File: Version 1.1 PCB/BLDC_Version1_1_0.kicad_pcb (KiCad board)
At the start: 2 copper layers, 80 x 80 mm, 122 parts, among them CN1 DB910-7.62-3P, CN2 XT60PW-M, CN3 SM06B-GHS-TB(LF)(SN), J1 USB_C_Receptacle_USB2.0_14P, Q1 N_FET_ISC0602NLS, Q2 N_FET_ISC0602NLS, Q3 SI7129DN-T1-GE3, Q4 N_FET_ISC0602NLS, Q5 N_FET_ISC0602NLS, Q6 N_FET_ISC0602NLS, Q7 N_FET_ISC0602NLS, SW1 SW_MEC_5E, SW2 SW_MEC_5E, U1 ESP32-S3-WROOM-1, U10 SRV05-4-HXY, U11 SRV05-4-HXY, U13 SRV05-4-HXY, U14 SRV05-4-HXY, U2 AP7363-33D-13, U3 TMC6200-TA-T, U4 TPS5430DDAR, U5 SM03B-GHS-TB(LF)(SN), U7 8x Male Headers, U9 Male Headers

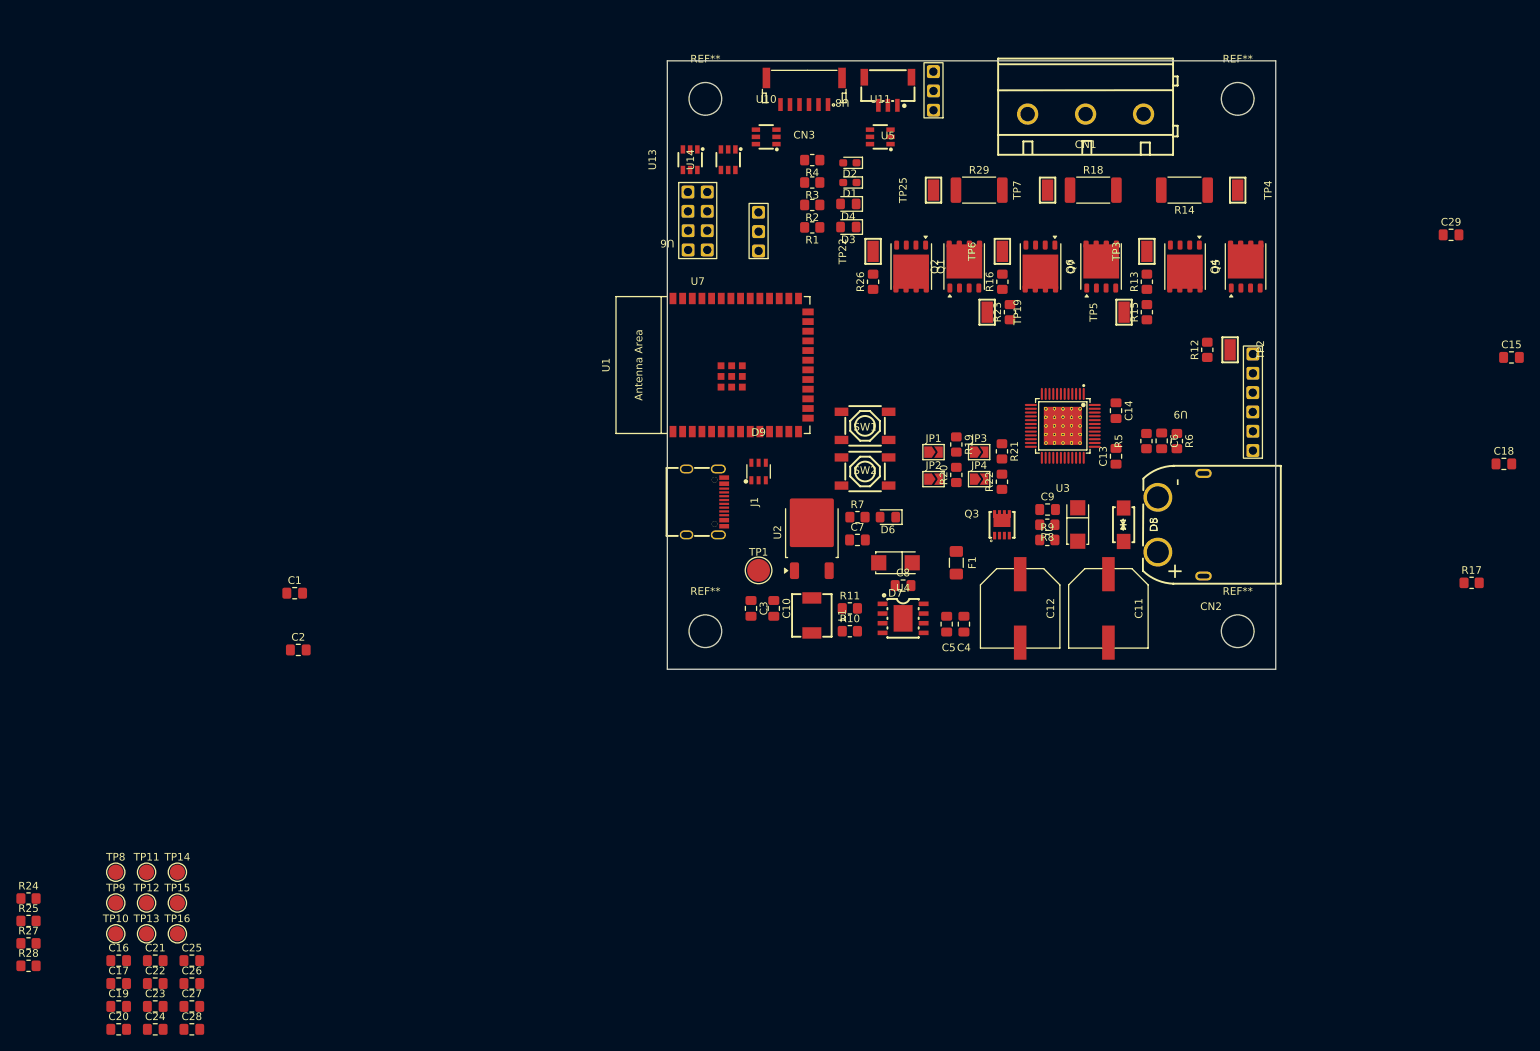
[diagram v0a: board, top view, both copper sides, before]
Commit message: Completed Placement of Parts
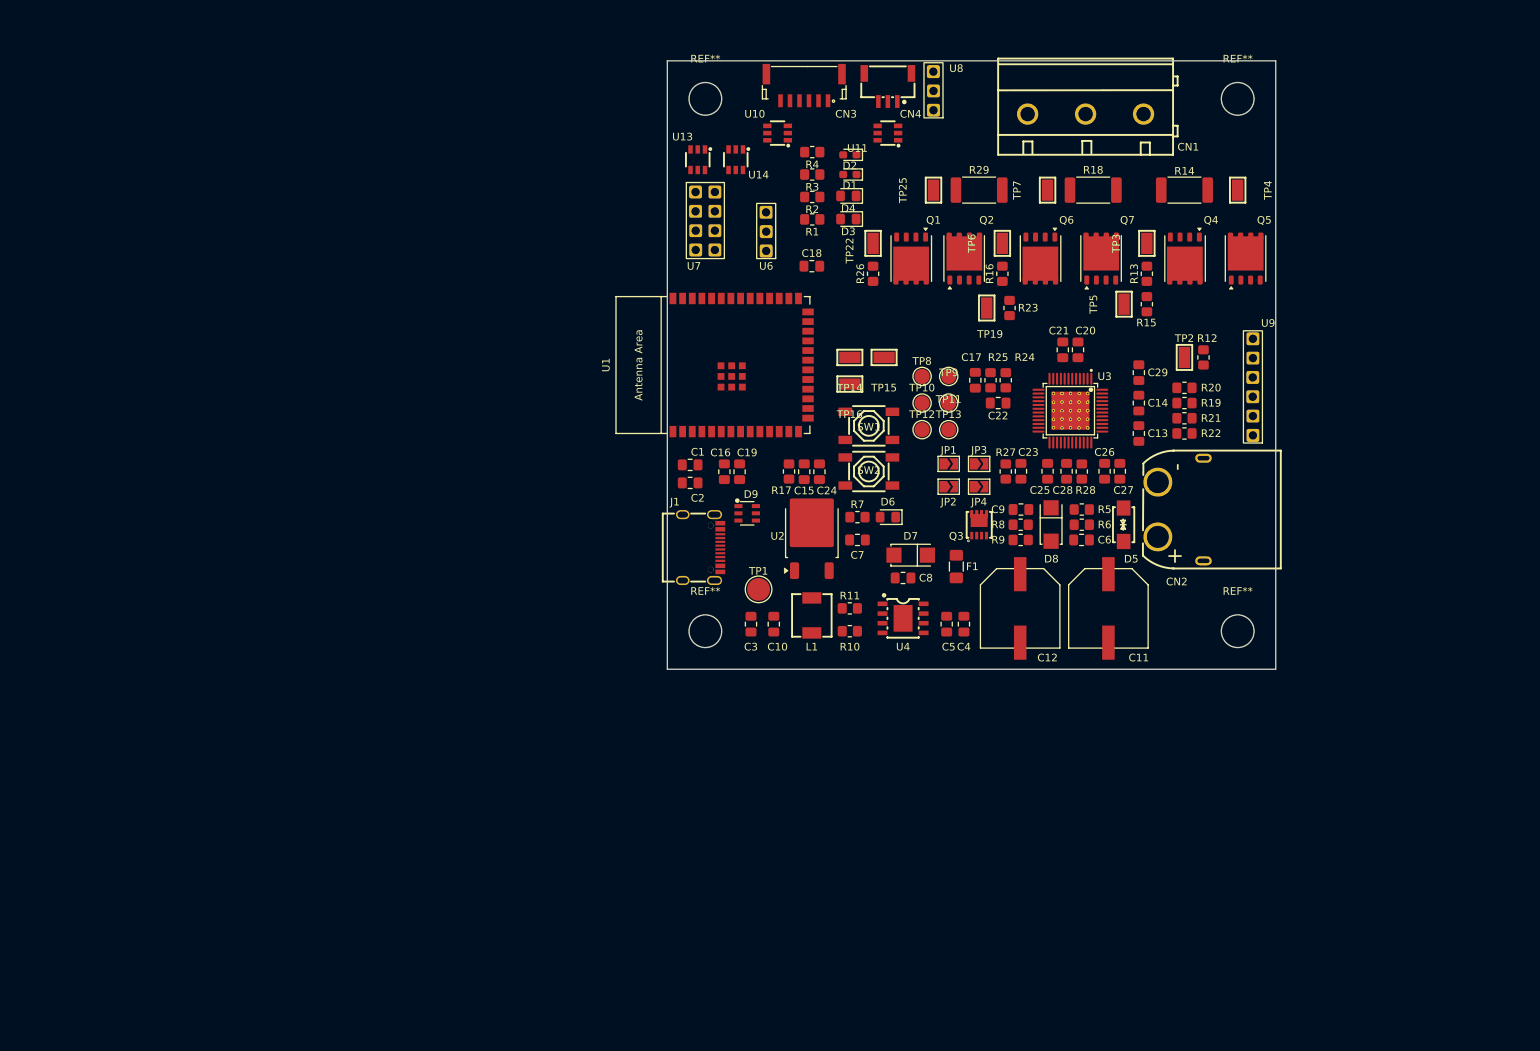
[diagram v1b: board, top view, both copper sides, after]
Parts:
- TP14, TP15, TP16: footprint TestPoint:TestPoint_Pad_D2.0mm -> easyeda2kicad:SMD_RH-5015
- moved C20 154.6 mm to (164.0, 98.0), turned to 90 degrees
- moved R28 153.0 mm to (164.5, 114.0), turned to 90 degrees
- moved R24 145.5 mm to (154.5, 102.0), turned to 90 degrees
- moved R25 145.1 mm to (152.5, 102.0), turned to -90 degrees
- moved C21 143.8 mm to (162.0, 98.0), turned to 90 degrees
- moved R27 142.7 mm to (154.5, 114.0), turned to -90 degrees
- moved C27 140.9 mm to (169.5, 114.0), turned to 90 degrees
- moved C17 137.8 mm to (150.5, 102.0), turned to -90 degrees
- moved C26 137.6 mm to (167.5, 114.0), turned to -90 degrees
- moved C28 136.4 mm to (162.5, 114.0), turned to -90 degrees
- moved C22 134.6 mm to (153.5, 105.0), turned to 180 degrees
- moved C23 133.8 mm to (156.5, 114.0), turned to -90 degrees
- moved C25 129.6 mm to (160.0, 114.0), turned to -90 degrees
- moved TP9 129.6 mm to (147.0, 101.5)
- moved TP10 126.9 mm to (143.5, 105.0)
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- renumbered U5 to CN4
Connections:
- U11 pad 1: GPIO35 -> GPIO37
- U11 pad 4: GPIO37 -> GPIO35
- U11 pad 6: GPIO01 -> unconnected-(U11-Pad6)
- U13 pad 1: GPIO43 -> GPIO16
- U13 pad 6: GPIO16 -> GPIO01
- U14 pad 3: GPIO47 -> GPIO43
- U14 pad 6: unconnected-(U14-Pad6) -> GPIO47

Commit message: began working on the routing
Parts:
- moved C6 4.26 mm to (164.8, 118.8)
- moved R5 3.76 mm to (164.8, 122.8)
- moved C18 3.02 mm to (131.8, 88.2), turned to 90 degrees
- moved R10 3.00 mm to (134.0, 132.0)
- moved R11 3.00 mm to (134.0, 135.0)
- moved TP2 2.51 mm to (180.5, 98.8)
- moved C1 2.49 mm to (113.0, 115.6), turned to 180 degrees
- moved R12 2.26 mm to (178.2, 98.8)
- moved C2 2.25 mm to (113.0, 113.2), turned to 180 degrees
- moved D7 1.35 mm to (140.8, 125.5)
- moved C20 1.03 mm to (163.8, 97.0)
- moved C21 1.03 mm to (161.8, 97.0)
- moved C8 0.91 mm to (140.9, 128.9)
- moved U10 0.79 mm to (123.8, 69.8)
- moved Q3 0.75 mm to (150.2, 121.0), turned to 90 degrees
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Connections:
- D9 pad 1: USB_D - -> USB_D +
- D9 pad 3: USB_D + -> USB_D -
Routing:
- net V_SENSE: track 0.00 -> 63.8 mm, vias 0 -> 1
- net GND: track 0.00 -> 63.6 mm, vias 0 -> 138
- net LIPO_VOLT_SENS: track 0.00 -> 57.8 mm, vias 0 -> 2
- net U_SENSE: track 0.00 -> 54.6 mm, vias 0 -> 1
- net W_SENSE: track 0.00 -> 47.9 mm, vias 0 -> 1
- net GPIO16: track 0.00 -> 46.5 mm, vias 0 -> 1
- net GPIO35: track 0.00 -> 46.4 mm, vias 0 -> 2
- net GPIO18: track 0.00 -> 44.6 mm, vias 0 -> 1
- net CURRENT_W: track 0.00 -> 44.6 mm
- net GPIO17: track 0.00 -> 42.4 mm, vias 0 -> 1
- net U_HIGHSIDE_GATE: track 0.00 -> 41.7 mm, vias 0 -> 2
- net GPIO36: track 0.00 -> 40.9 mm, vias 0 -> 2
- net GPIO37: track 0.00 -> 39.8 mm, vias 0 -> 2
- net LIPO_FAULT: track 0.00 -> 39.4 mm, vias 0 -> 2
- net USB_D +: track 0.00 -> 38.0 mm
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- added copper zone on F.Cu, net /Power Management/SOFTSTART_PWR_IN
- added copper zone on F.Cu, net 16.8V_BUS
- added copper zone on In2.Cu, net 16.8V_BUS
- added copper zone on In2.Cu, net 3.3V_BUS
- added copper zone on F.Cu, net 5V_BUS
- added copper zone on F.Cu, net DRIVER_U
- added copper zone on F.Cu, net DRIVER_V
- added copper zone on F.Cu, net DRIVER_W
- added copper zone on B.Cu, net GND
- added copper zone on F.Cu, net GND
- added copper zone on In1.Cu, net GND
- added copper zone on F.Cu, net Net-(U4-VSENSE)
- added copper zone on F.Cu, net U_SENSE
- added copper zone on F.Cu, net V_SENSE
- added copper zone on F.Cu, net W_SENSE
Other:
- copper layers 2 -> 4

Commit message: worked on traces
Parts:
- moved R12 3.58 mm to (174.8, 98.0), turned to 0 degrees
- turned R11 to 180 degrees
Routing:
- net V_SENSE: track 63.8 -> 49.3 mm
- net 16.8V_BUS: track 22.8 -> 32.1 mm
- net U_SENSE: track 54.6 -> 45.4 mm
- net Net-(U3-SPE): track 0.00 -> 7.29 mm
- net GND: track 63.6 -> 56.7 mm
- net VOLTAGE_CHARGE_PUMP: track 0.00 -> 6.57 mm
- net Net-(Q5-G): track 13.0 -> 18.1 mm
- net W_LOWSIDE_GATE: track 15.3 -> 10.9 mm
- net DRV_FAULT: track 29.1 -> 33.3 mm, vias 0 -> 1
- net CHARGE_CAPACITOR_INPUT: track 0.00 -> 3.61 mm
- net CHARGE_CAPACITOR_OUTPUT: track 0.00 -> 3.34 mm
- net DRIVER_SCK/IDRV1: track 0.00 -> 2.61 mm, vias 0 -> 1
- net DRIVER_U: track 35.4 -> 32.9 mm
- net DRV_ENABLE: track 0.00 -> 2.46 mm, vias 0 -> 1
- net DRIVER_SDO/SINGLE: track 0.00 -> 2.40 mm, vias 0 -> 1
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
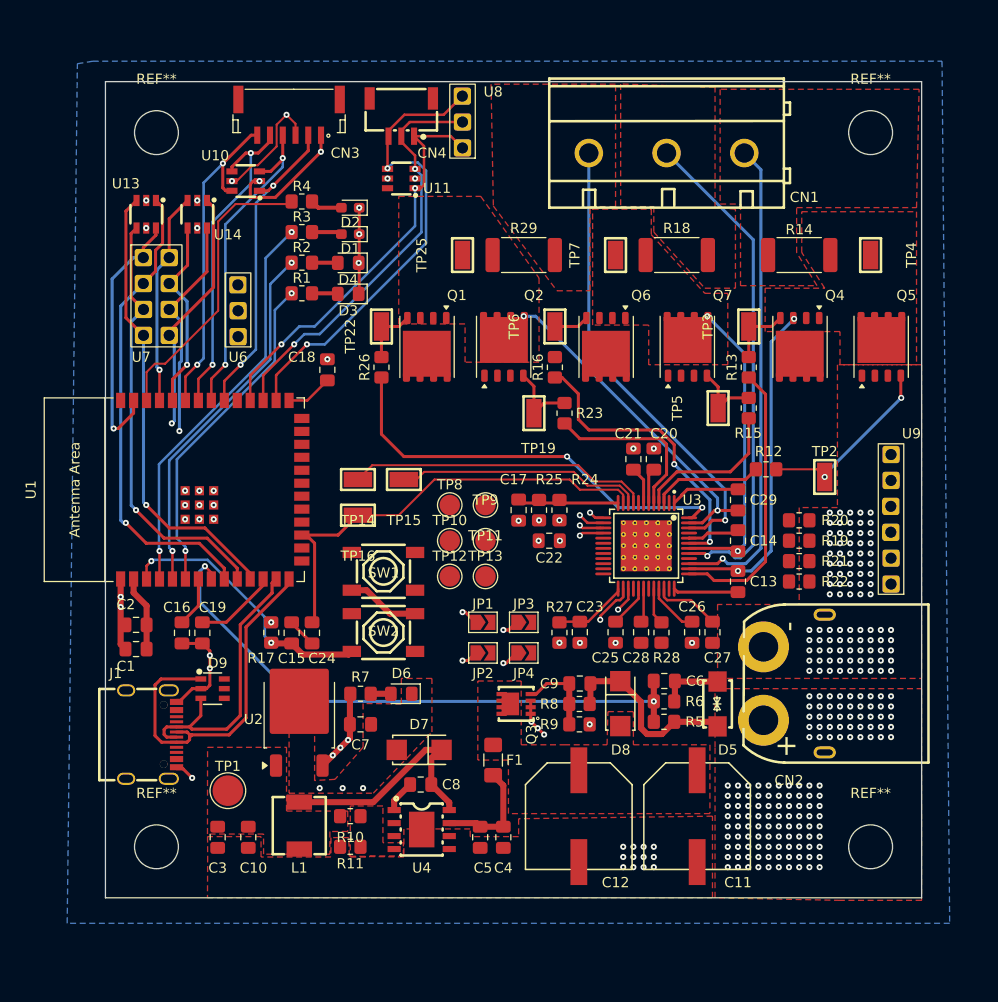
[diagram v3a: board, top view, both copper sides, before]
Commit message: Routing Complete
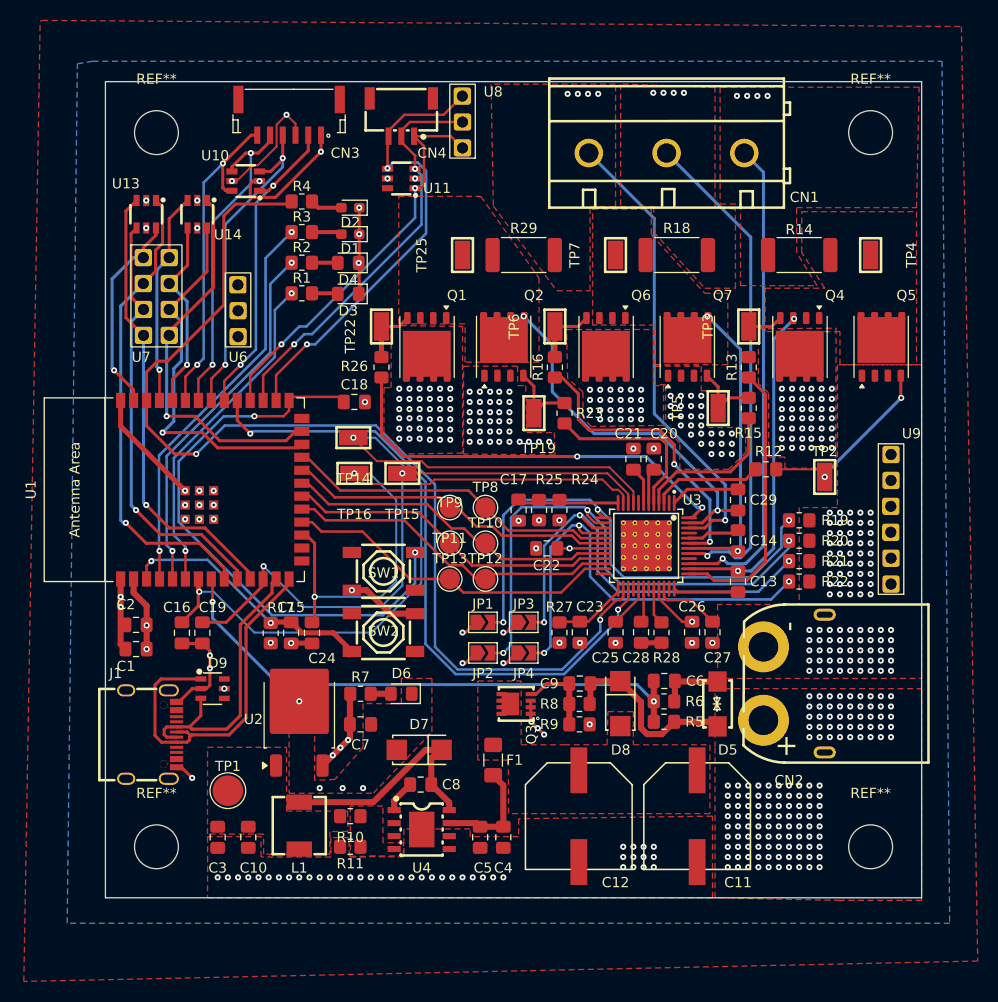
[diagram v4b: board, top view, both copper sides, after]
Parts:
- moved TP14 4.12 mm to (134.3, 94.9)
- moved C18 4.12 mm to (134.4, 91.4), turned to 0 degrees
- moved TP16 4.11 mm to (134.4, 98.4)
- moved TP10 3.51 mm to (147.2, 105.2)
- moved TP11 3.51 mm to (143.8, 105.2)
- moved TP12 3.51 mm to (147.2, 108.8)
- moved TP13 3.51 mm to (143.8, 108.8)
- moved TP8 3.51 mm to (147.2, 101.8)
- moved TP9 3.51 mm to (143.8, 101.8)
- moved R19 2.00 mm to (178.0, 103.0)
- moved R20 2.00 mm to (178.0, 105.0)
- moved C22 0.79 mm to (153.2, 105.8)
- moved TP15 0.62 mm to (139.1, 98.4)
- moved R17 0.08 mm to (126.2, 114.1), turned to 90 degrees
- moved C15 0.05 mm to (128.2, 114.0), turned to -90 degrees
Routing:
- net DRV_FAULT: track 33.3 -> 104.4 mm, vias 1 -> 2
- net DRV_ENABLE: track 2.46 -> 64.8 mm, vias 1 -> 2
- net BOOT: track 4.62 -> 57.0 mm, vias 0 -> 2
- net DRIVER_SCK/IDRV1: track 2.61 -> 52.5 mm, vias 1 -> 3
- net DRIVER_CSN/IDRV0: track 1.51 -> 50.6 mm, vias 1 -> 3
- net CURRENT_U: track 34.6 -> 79.5 mm, vias 0 -> 2
- net DRIVER_SDO/SINGLE: track 2.40 -> 45.3 mm, vias 1 -> 3
- net DRIVER_SDI/AMPL: track 2.40 -> 43.5 mm, vias 1 -> 3
- net W_LOWSIDE: track 0.00 -> 33.4 mm
- net U_LOWSIDE: track 0.00 -> 33.0 mm
- net W_HIGHSIDE: track 0.00 -> 33.0 mm
- net V_HIGHSIDE: track 0.00 -> 32.9 mm
- net U_HIGHSIDE: track 0.00 -> 32.8 mm
- net V_LOWSIDE: track 0.00 -> 32.6 mm
- net CURRENT_V: track 32.2 -> 60.3 mm, vias 0 -> 2
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
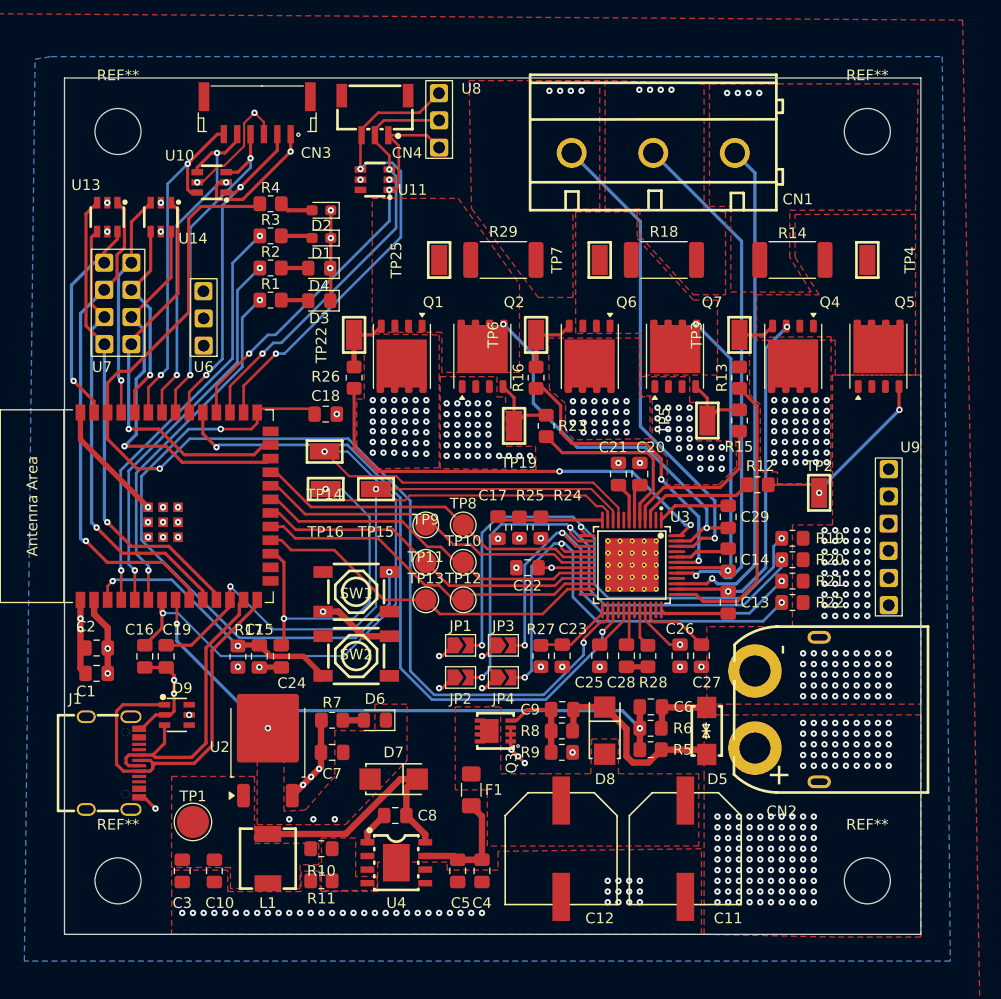
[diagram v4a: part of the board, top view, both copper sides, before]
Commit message: Added silkscreen texts and logo
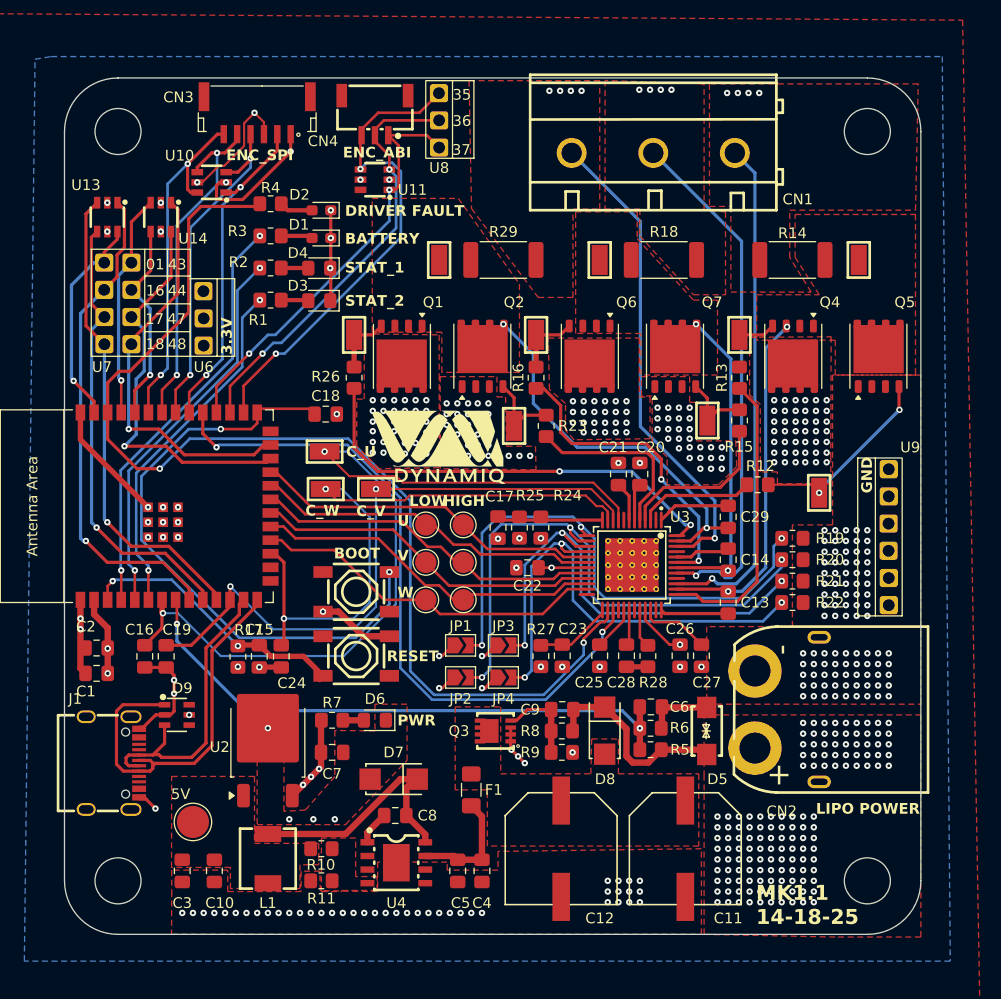
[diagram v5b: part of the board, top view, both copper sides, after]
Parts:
- added G***: LOGO, Project_BLDC_Foorprint_Library:LOGO, F.Cu at (145.3, 94.3)
- added G***: LOGO, Project_BLDC_Foorprint_Library:LOGO_LARGE, B.Cu at (158.6, 130.4)
- moved TP4 0.80 mm to (184.2, 77.0)
- renumbered TP1 to 5V
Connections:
- R17 pad 1: +3.3V -> 3.3V_BUS
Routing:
- net 3.3V_BUS: vias 17 -> 18
- net +3.3V: vias 1 -> 0
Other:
- outline, holes or cut-outs redrawn
- board text added: "01"
- board text added: "16"
- board text added: "17"
- board text added: "18"
- board text added: "3.3V"
- board text added: "35"
- board text added: "36"
- board text added: "37"
- board text added: "43"
- board text added: "44"
- board text added: "47"
- board text added: "48"
- board text added: "BATTERY"
- board text added: "BOOT"
- board text added: "C_U"
- board text added: "C_V"
- board text added: "C_W"
- board text added: "DRIVER FAULT"
- board text added: "ENC_ABI"
- board text added: "ENC_SPI"
- board text added: "GND"
- board text added: "HIGH"
- board text added: "LIPO POWER"
- board text added: "LOW"
- board text added: "MK 1.1 BLDC Controller Designed by David 14-08-2025"
- board text added: "MK1.1 14-18-25"
- board text added: "PWR"
- board text added: "RESET"
- board text added: "STAT_1"
- board text added: "STAT_2"
- board text added: "U"
- board text added: "V"
- board text added: "W"
